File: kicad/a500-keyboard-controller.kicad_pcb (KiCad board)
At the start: 2 copper layers, 168 x 39.5 mm, 38 parts, among them J1 ICSP, J2 keyboard_matrix, J3 Mainboard, Q1 BC547, U1 PIC18F4520

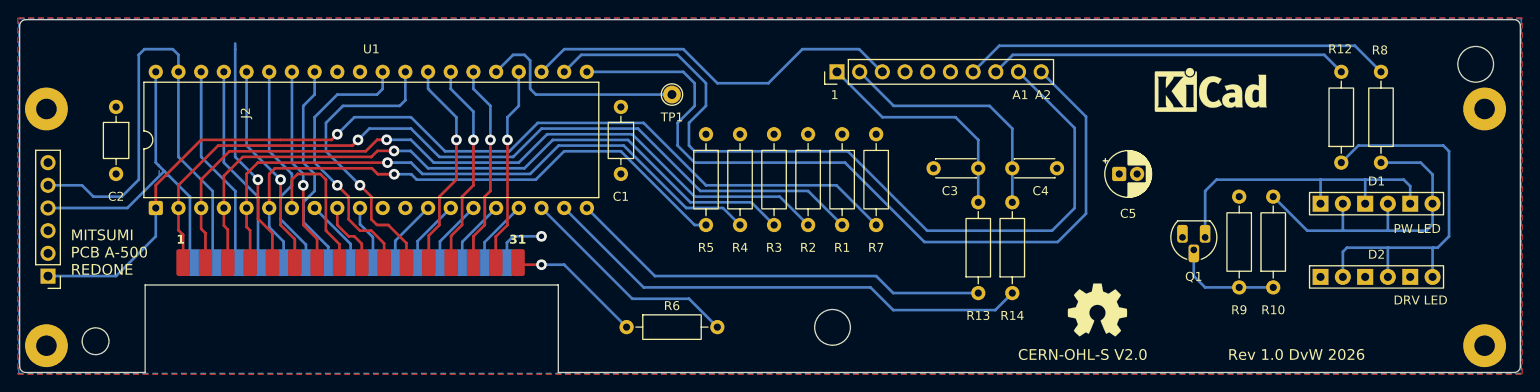
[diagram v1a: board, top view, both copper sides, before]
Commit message: larger margin around ground pads
Moved ICSP connector
added teardrops to SMD pads
optimized some tracks so we can move host cable connector
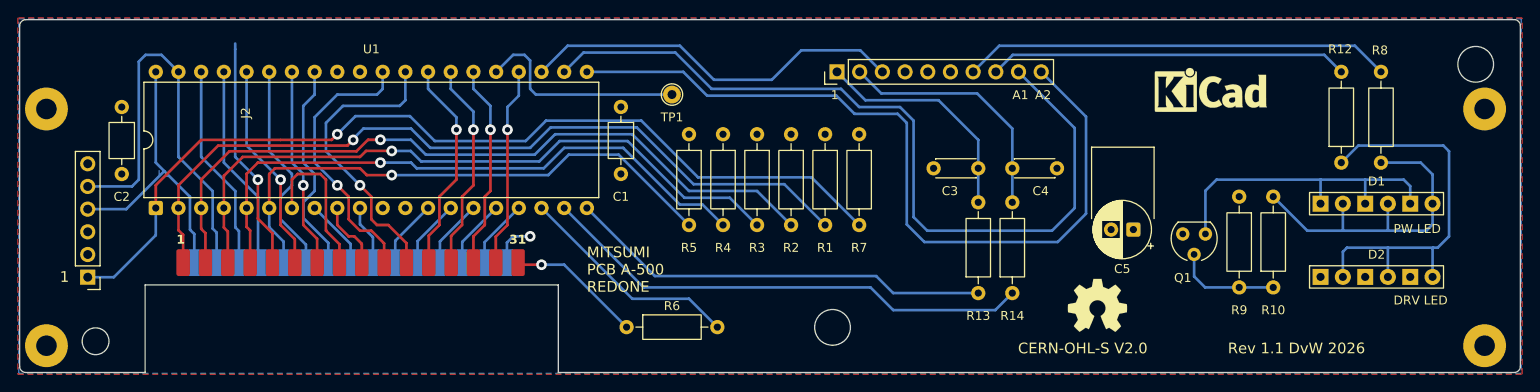
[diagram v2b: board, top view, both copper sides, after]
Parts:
- C5: footprint Capacitor_THT:CP_Radial_D5.0mm_P2.00mm -> Capacitor_THT:CP_Radial_D6.3mm_P2.50mm
- moved C5 6.42 mm to (197.1, 107.4), turned to 180 degrees
- moved J1 4.45 mm to (80.0, 112.7)
- moved R2 1.91 mm to (158.8, 96.7)
- moved R1 1.91 mm to (162.6, 96.7)
- moved R3 1.91 mm to (154.9, 96.7)
- moved R4 1.91 mm to (151.1, 96.7)
- moved R5 1.91 mm to (147.3, 96.7)
- moved R7 1.91 mm to (166.4, 96.7)
- moved Q1 1.24 mm to (203.9, 108.4)
- moved C2 0.64 mm to (83.8, 93.7)
- moved REF2 0.52 mm to (193.1, 115.9)
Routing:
- net ~{X7}/PGC: track 55.4 -> 47.9 mm
- net ~{MCLR}: track 111.1 -> 104.0 mm
- net ~{X5}/PGD: track 37.9 -> 33.5 mm
- net ~{X6}: track 85.9 -> 83.2 mm
- net ~{X3}: track 78.7 -> 76.1 mm
- net ~{X2}: track 71.4 -> 68.7 mm
- net ~{RAMI}: track 65.0 -> 62.4 mm
- net ~{X4}: track 92.9 -> 90.3 mm
- net GND: track 6.40 -> 5.13 mm
- net Net-(Q1-B): track 12.3 -> 11.8 mm
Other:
- board text added: "Rev 1.1 DvW 2026"
- board text removed: "Rev 1.0 DvW 2026"

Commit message: host cable now connects to right angle pin header
This is version 1.1 and has been sent to production
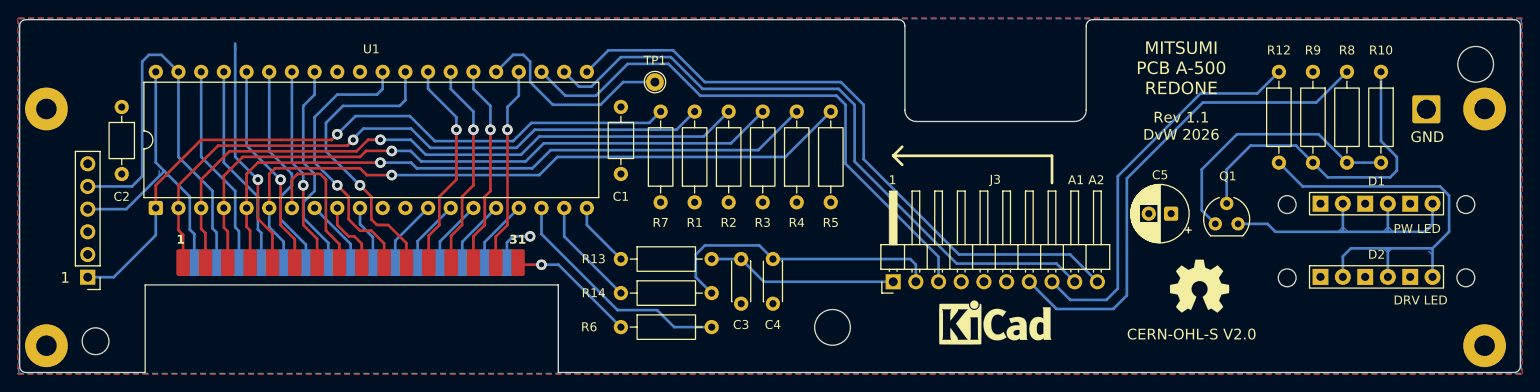
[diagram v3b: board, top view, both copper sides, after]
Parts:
- added J4: EARTH_STRAP, Connector_Wire:SolderWire-1.5sqmm_1x01_D1.7mm_OD3mm, F.Cu at (229.9, 93.9)
- J3: footprint Connector_PinHeader_2.54mm:PinHeader_1x10_P2.54mm_Vertical -> Connector_PinHeader_2.54mm:PinHeader_1x10_P2.54mm_Horizontal
- R10: value 1K8 -> 3K3
- R9: value 470R -> 4K7
- moved R14 43.8 mm to (139.7, 114.5), turned to 0 degrees
- moved R13 40.2 mm to (139.7, 110.7), turned to 0 degrees
- moved REF1 35.5 mm to (181.6, 118.3)
- moved C4 28.7 mm to (156.7, 110.7), turned to -90 degrees
- moved C3 28.4 mm to (153.2, 110.7), turned to -90 degrees
- moved R10 27.0 mm to (224.8, 89.7), turned to -90 degrees
- moved J3 24.3 mm to (170.2, 113.2)
- moved R7 23.5 mm to (144.2, 104.3), turned to 90 degrees
- moved R5 17.6 mm to (163.2, 104.3), turned to 90 degrees
- moved R1 16.5 mm to (148.0, 104.3), turned to 90 degrees
- moved R9 16.2 mm to (217.2, 89.7)
- moved REF2 11.6 mm to (204.5, 113.7)
- moved R4 11.2 mm to (159.4, 104.3), turned to 90 degrees
- moved R2 10.3 mm to (151.8, 104.4), turned to 90 degrees
- moved R3 7.65 mm to (155.6, 104.3), turned to 90 degrees
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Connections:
- D1 pad 1: Net-(D1A-K) -> GND
- D1 pad 3: Net-(D1A-K) -> GND
- D1 pad 5: Net-(D1A-K) -> GND
- Q1 pad 1: Net-(D1A-K) -> Net-(Q1-C)
- Q1 pad 3: GND -> Net-(D1A-A)
- R10 pad 2: Net-(D1A-A) -> Net-(Q1-C)
- R8 pad 1: Net-(D1A-A) -> Net-(Q1-C)
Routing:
- net KDAT: track 55.7 -> 12.2 mm
- net KCLK: track 47.8 -> 7.29 mm
- net Net-(D1A-K): track 35.9 -> 0.00 mm
- net Net-(Q1-C): track 0.00 -> 29.7 mm
- net ~{MCLR}: track 104.0 -> 77.4 mm
- net Net-(Q1-B): track 11.8 -> 37.5 mm
- net ~{RST}: track 43.3 -> 62.6 mm
- net ~{X4}: track 90.3 -> 71.9 mm
- net AUX1: track 91.5 -> 73.3 mm
- net AUX2: track 89.7 -> 72.5 mm
- net ~{RAMI}: track 62.4 -> 77.0 mm
- net ~{X6}: track 83.2 -> 73.1 mm
- net PWR_LED: track 48.1 -> 55.5 mm
- net Net-(D1A-A): track 37.7 -> 31.1 mm
- net ~{X2}: track 68.7 -> 75.1 mm
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- added copper zone on B.Cu, net Net-(D1A-A)
- added copper zone on B.Cu, net Net-(D2A-A)
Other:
- outline, holes or cut-outs redrawn
- board text added: "GND"

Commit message: - fixed LED footprint dimensions
- completely reworked power LED circuit
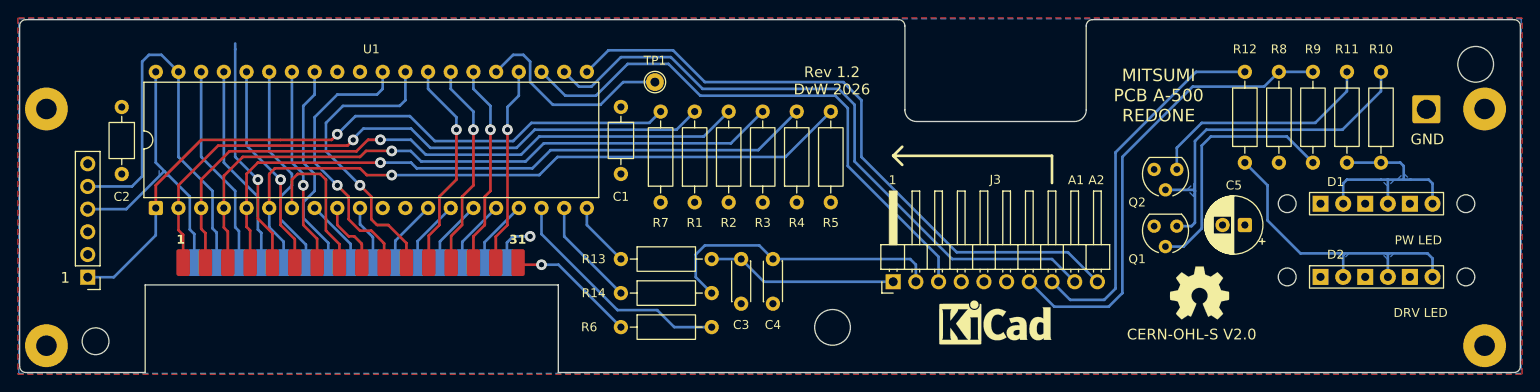
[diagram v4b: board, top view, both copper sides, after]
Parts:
- added Q2: BC557, Library:TO-92_HandSolder_modified, F.Cu at (200.7, 101.2)
- added R11: 1k8, Resistor_THT:R_Axial_DIN0207_L6.3mm_D2.5mm_P10.16mm_Horizontal, F.Cu at (221.0, 99.9)
- Q1: value BC547 -> BC557
- R10: value 3K3 -> 8K2
- R8: value 22R -> 390R
- R9: value 4K7 -> 10K
- moved R10 10.2 mm to (224.8, 99.9), turned to 90 degrees
- moved R9 10.2 mm to (217.2, 99.9), turned to 90 degrees
- moved C5 8.35 mm to (209.6, 106.9)
- moved R8 7.62 mm to (213.4, 99.9)
- moved Q1 6.97 mm to (200.7, 107.5), turned to 180 degrees
- moved R12 3.81 mm to (209.6, 99.9)
- moved REF2 0.76 mm to (204.5, 114.5)
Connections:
- Q1 pad 3: Net-(D1A-A) -> VDD
- R10 pad 1: Net-(Q1-B) -> Net-(D1A-A)
- R8 pad 1: Net-(Q1-C) -> GND
- R9 pad 1: GND -> Net-(Q1-B)
- R9 pad 2: Net-(Q1-B) -> PWR_LED
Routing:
- net Net-(Q2-C): track 0.00 -> 26.3 mm
- net Net-(D2A-A): track 46.4 -> 35.2 mm
- net Net-(Q1-C): track 29.7 -> 40.0 mm
- net Net-(Q1-B): track 37.5 -> 28.3 mm
- net Net-(D1A-A): track 31.1 -> 25.6 mm
- net PWR_LED: track 55.5 -> 52.7 mm
- net DRV_LED: track 44.2 -> 41.9 mm
- added copper zone on B.Cu, net Net-(Q1-C)
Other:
- board text added: "Rev 1.2 DvW 2026"
- board text removed: "Rev 1.1 DvW 2026"

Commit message: moved OSHW logo a bit, this version sent to fabrication
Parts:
- moved REF2 0.25 mm to (204.5, 114.3)

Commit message: changed LED current limiting resistors values
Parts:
- R10: value 8K2 -> 6K8
- R12: value 270R -> 470R
